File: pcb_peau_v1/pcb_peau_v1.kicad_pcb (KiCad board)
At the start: 2 copper layers, 76 x 74 mm, 27 parts, among them J1 Conn_01x05, J2 Conn_01x05, J4 Conn_02x08_Top_Bottom, J5 Conn_02x12_Top_Bottom, U1 REF200AU, U2 TLC274, U3 CD74HC4067SM, U4 CD74HC4067SM, U5 CD74HC4067SM, U6 CD74HC4067SM, U7 TLC274, U8 TLC274, U9 TLC274

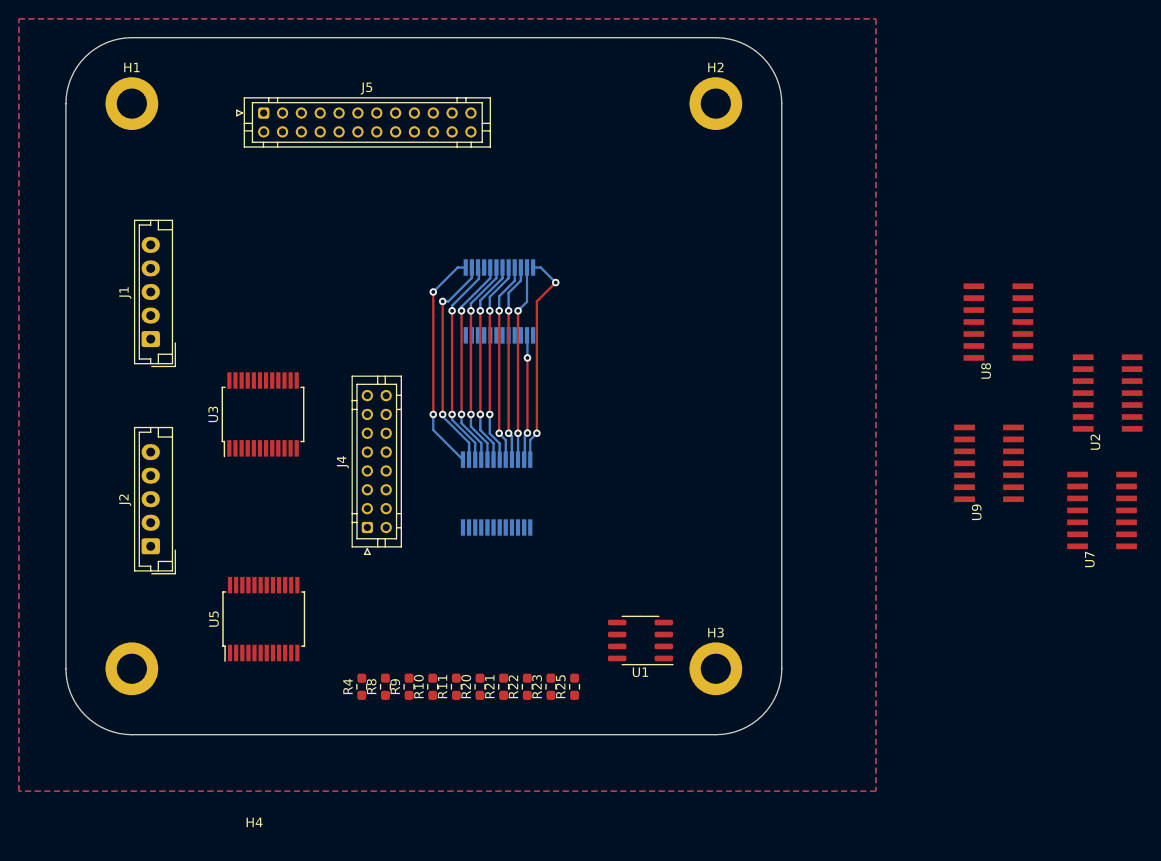
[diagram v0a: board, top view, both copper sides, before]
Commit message: PCB Mux/demux
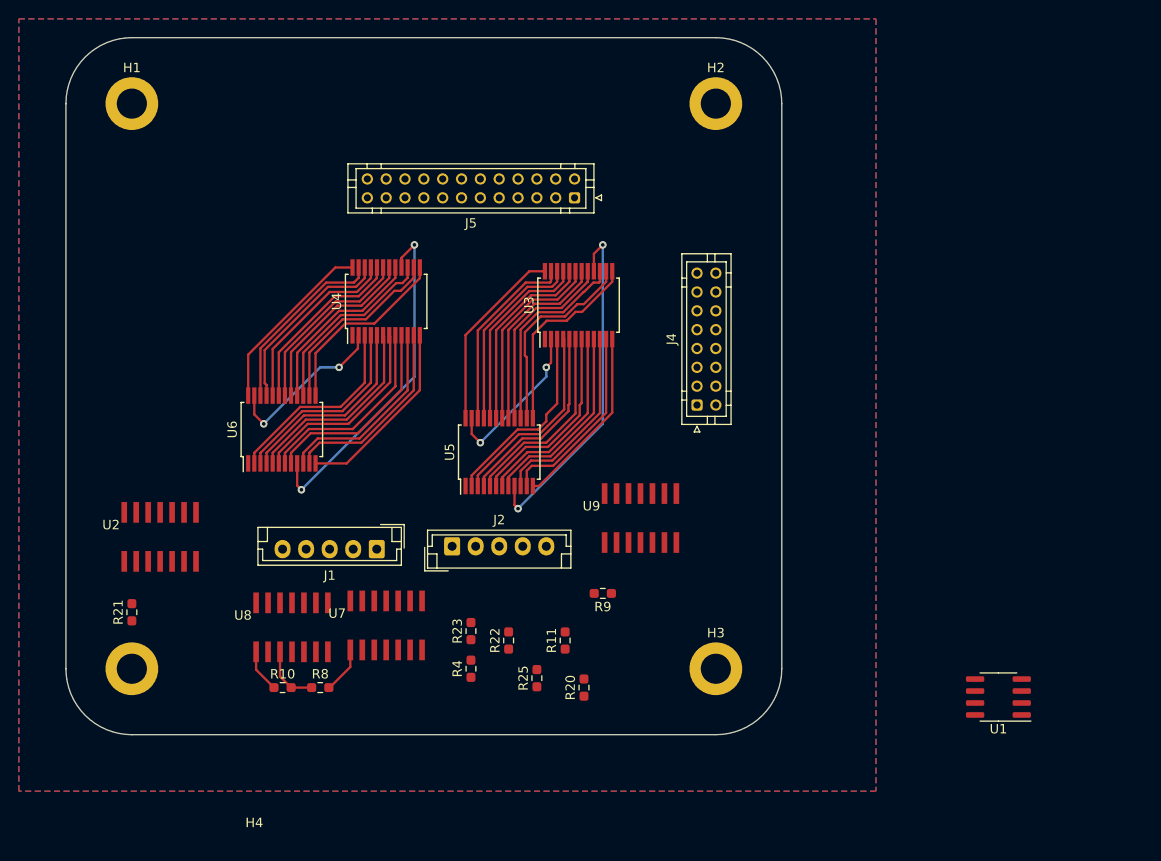
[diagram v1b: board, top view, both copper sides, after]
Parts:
- U4, U6: moved to F.Cu
- moved U2 101.8 mm to (177.0, 96.0), turned to 0 degrees
- moved U8 81.7 mm to (191.0, 105.6), turned to 0 degrees
- moved U7 77.0 mm to (201.0, 105.4), turned to 0 degrees
- moved R21 40.3 mm to (174.0, 104.0)
- moved U1 38.5 mm to (266.0, 113.0)
- moved U9 37.5 mm to (228.0, 94.0), turned to 0 degrees
- moved J4 37.3 mm to (234.0, 82.0)
- moved U3 35.5 mm to (221.4, 71.4)
- moved J5 34.2 mm to (221.0, 60.0), turned to 180 degrees
- moved J1 32.8 mm to (200.0, 97.3), turned to 180 degrees
- moved J2 32.0 mm to (208.0, 97.0), turned to 0 degrees
- moved U5 30.6 mm to (213.0, 87.0)
- moved U6 23.8 mm to (189.9, 84.6)
- moved R9 22.8 mm to (224.0, 102.0), turned to 180 degrees
- moved R10 15.9 mm to (190.0, 112.0), turned to 0 degrees
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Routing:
- net Net-(J4-Pin_1): track 0.00 -> 74.4 mm, vias 0 -> 4
- net Net-(J4-Pin_2): track 0.00 -> 42.1 mm
- net Net-(J4-Pin_3): track 0.00 -> 41.9 mm
- net Net-(J4-Pin_5): track 0.00 -> 41.8 mm
- net Net-(J4-Pin_4): track 0.00 -> 41.8 mm
- net Net-(J4-Pin_7): track 0.00 -> 41.7 mm
- net Net-(J4-Pin_8): track 0.00 -> 41.6 mm
- net Net-(J4-Pin_6): track 0.00 -> 41.5 mm
- net 0: track 0.00 -> 39.6 mm
- net Net-(J4-Pin_9): track 13.4 -> 35.2 mm, vias 2 -> 4
- net C1: track 0.00 -> 21.2 mm
- net NE1: track 0.00 -> 21.0 mm
- net A2: track 0.00 -> 20.8 mm
- net B2: track 0.00 -> 20.8 mm
- net D1: track 0.00 -> 20.7 mm
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
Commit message: PCB avancé
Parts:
- moved J4 24.3 mm to (210.0, 86.0)
- moved U5 8.92 mm to (221.9, 86.3)
- moved U3 8.92 mm to (230.3, 70.7)
- moved U9 8.49 mm to (234.0, 100.0)
- moved U4 1.48 mm to (201.3, 72.5)
- moved U6 1.48 mm to (190.2, 86.0)
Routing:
- net Net-(J4-Pin_7): track 41.7 -> 100.1 mm, vias 0 -> 3
- net Net-(J4-Pin_10): track 40.0 -> 98.1 mm, vias 0 -> 2
- net Net-(J4-Pin_15): track 39.8 -> 91.1 mm, vias 0 -> 2
- net Net-(J4-Pin_4): track 41.8 -> 92.0 mm, vias 0 -> 1
- net Net-(J4-Pin_14): track 39.8 -> 89.4 mm, vias 0 -> 2
- net Net-(J4-Pin_13): track 39.8 -> 89.1 mm, vias 0 -> 2
- net Net-(J4-Pin_5): track 41.8 -> 90.6 mm, vias 0 -> 1
- net Net-(J4-Pin_12): track 40.0 -> 88.2 mm, vias 0 -> 2
- net Net-(J4-Pin_3): track 41.9 -> 89.0 mm
- net Net-(J4-Pin_11): track 40.2 -> 86.9 mm
- net Net-(J4-Pin_8): track 41.6 -> 86.8 mm, vias 0 -> 3
- net Net-(J4-Pin_2): track 42.1 -> 87.2 mm, vias 0 -> 1
- net Net-(J4-Pin_16): track 39.8 -> 84.3 mm, vias 0 -> 2
- net Net-(J4-Pin_9): track 35.2 -> 70.0 mm, vias 4 -> 6
- net Net-(J4-Pin_6): track 41.5 -> 75.6 mm
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
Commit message: fin
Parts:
- removed R20: 1M, Resistor_SMD:R_0603_1608Metric_Pad0.98x0.95mm_HandSolder
- removed U1: REF200AU, Package_SO:SOIC-8_3.9x4.9mm_P1.27mm
- moved R21 48.4 mm to (222.3, 101.4), turned to 0 degrees
- moved J1 33.6 mm to (178.0, 72.0), turned to -90 degrees
- moved J2 32.7 mm to (237.0, 82.0), turned to 90 degrees
- moved J5 30.9 mm to (216.0, 90.5)
- moved U2 26.0 mm to (203.0, 96.5)
- moved R25 23.1 mm to (196.0, 101.5), turned to 180 degrees
- moved R10 15.5 mm to (181.6, 98.9), turned to -90 degrees
- moved R8 15.4 mm to (181.6, 102.9), turned to -90 degrees
- moved R11 10.9 mm to (210.2, 102.3)
- moved R9 9.83 mm to (214.2, 102.4), turned to -90 degrees
- moved R23 9.10 mm to (218.3, 102.4)
- moved U5 8.77 mm to (219.9, 77.7)
- moved U4 8.77 mm to (199.3, 63.9)
- moved J4 8.77 mm to (208.0, 77.5)
- moved U3 8.77 mm to (228.3, 62.1)
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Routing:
- net +5V: track 39.3 -> 190.1 mm, vias 0 -> 7
- net AOP1: track 0.00 -> 85.8 mm, vias 0 -> 4
- net AOP2: track 0.00 -> 66.0 mm, vias 0 -> 2
- net +12V: track 0.00 -> 60.8 mm, vias 0 -> 1
- net -5V: track 0.00 -> 59.5 mm, vias 0 -> 2
- net NE2: track 20.0 -> 74.1 mm, vias 0 -> 3
- net AOP0IN+: track 0.00 -> 52.4 mm, vias 0 -> 1
- net C2: track 20.0 -> 58.6 mm, vias 0 -> 1
- net Net-(U9A-+): track 0.00 -> 33.8 mm
- net Net-(U8A--): track 0.00 -> 30.8 mm, vias 0 -> 2
- net D1: track 20.7 -> 51.3 mm, vias 0 -> 1
- net Net-(U7A-+): track 4.99 -> 33.0 mm, vias 0 -> 2
- net D2: track 20.0 -> 47.6 mm, vias 0 -> 1
- net NE1: track 21.0 -> 46.2 mm, vias 0 -> 1
- net C1: track 21.2 -> 46.3 mm, vias 0 -> 1
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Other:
- board size 76 x 74 mm -> 72.1 x 71 mm

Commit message: PCB corrigé
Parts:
- added R20: 1M, Resistor_SMD:R_0603_1608Metric_Pad0.98x0.95mm_HandSolder, F.Cu at (196.1, 100.0)
- moved H3 1.00 mm to (236.0, 111.0)
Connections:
- J5 pad 10: unconnected-(J5-Pin_10-Pad10) -> C3
- J5 pad 11: unconnected-(J5-Pin_11-Pad11) -> D3
- J5 pad 13: unconnected-(J5-Pin_13-Pad13) -> A4
- J5 pad 14: unconnected-(J5-Pin_14-Pad14) -> B4
- J5 pad 15: unconnected-(J5-Pin_15-Pad15) -> C4
- J5 pad 16: unconnected-(J5-Pin_16-Pad16) -> D4
- J5 pad 8: unconnected-(J5-Pin_8-Pad8) -> A3
- J5 pad 9: unconnected-(J5-Pin_9-Pad9) -> B3
- U3 pad 10: A1 -> A3
- U3 pad 11: B1 -> B3
- U3 pad 13: D1 -> D3
- U3 pad 14: C1 -> C3
- U4 pad 10: A2 -> A4
- U4 pad 11: B2 -> B4
- U4 pad 13: D2 -> D4
- U4 pad 14: C2 -> C4
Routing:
- net D3: track 0.00 -> 58.0 mm, vias 0 -> 1
- net C3: track 0.00 -> 54.9 mm, vias 0 -> 1
- net B3: track 0.00 -> 46.9 mm, vias 0 -> 1
- net A3: track 0.00 -> 41.9 mm, vias 0 -> 2
- net C4: track 0.00 -> 35.5 mm, vias 0 -> 2
- net D4: track 0.00 -> 32.2 mm, vias 0 -> 4
- net A4: track 0.00 -> 25.5 mm
- net B4: track 0.00 -> 22.8 mm
- net D1: track 51.3 -> 28.7 mm
- net B1: track 35.1 -> 14.6 mm
- net A1: track 31.8 -> 11.3 mm
- net C2: track 58.6 -> 38.6 mm
- net Net-(R20-Pad1): track 0.00 -> 19.8 mm, vias 0 -> 2
- net D2: track 47.6 -> 28.2 mm
- net C1: track 46.3 -> 27.8 mm
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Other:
- board size 72.1 x 71 mm -> 70 x 70 mm

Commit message: Modif
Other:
- board text added: "PROJET PEAU_ARTIFICIELLE MITCHEL Maël TCHEGANG YANSE Picard"
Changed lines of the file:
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@@
   (gr_line (start 178 47) (end 236 47)
     (stroke (width 0.1) (type default)) (layer "Edge.Cuts"))
+  (gr_text "PROJET PEAU_ARTIFICIELLE\nMITCHEL Maël\nTCHEGANG YANSE Picard" (at 210 114) (layer "B.Cu")
+    (effects (font (size 1 1) (thickness 0.25) bold) (justify left bottom))
+  )
   (segment (start 203 69.4625) (end 202.848896 69.311396) (width 0.25) (layer "F.Cu") (net 1))
   (segment (start 202.848896 69.311396) (end 202.848896 67.5125) (width 0.25) (layer "F.Cu") (net 1))

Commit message: Pcb Corrigé presque pret
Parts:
- added J3: Conn_01x02, Connector_JST:JST_EH_B2B-EH-A_1x02_P2.50mm_Vertical, F.Cu at (225.1, 110.2)
- moved U7 18.4 mm to (184.7, 101.3)
- moved J5 17.0 mm to (218.7, 73.7)
- moved R8 15.3 mm to (193.0, 113.1)
- moved R10 14.9 mm to (188.5, 112.1)
- moved U2 14.7 mm to (216.9, 101.3)
- moved R20 12.6 mm to (200.7, 111.8)
- moved R25 12.6 mm to (200.6, 113.2)
- moved U8 11.5 mm to (200.9, 101.1), turned to 0 degrees
- moved J4 10.6 mm to (214.1, 86.1), turned to 180 degrees
- moved R21 9.81 mm to (217.9, 110.1), turned to -90 degrees
- moved U4 9.74 mm to (190.5, 59.7)
- moved U9 8.91 mm to (232.7, 101.3)
- moved U5 8.63 mm to (226.3, 83.5)
- moved R11 8.51 mm to (207.3, 110.3)
- moved R23 8.49 mm to (215.1, 110.2)
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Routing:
- net Net-(J4-Pin_9): track 68.5 -> 150.2 mm, vias 6 -> 4
- net Net-(J4-Pin_4): track 91.9 -> 163.2 mm, vias 1 -> 6
- net Net-(J4-Pin_11): track 87.6 -> 141.3 mm, vias 0 -> 7
- net 0: track 45.3 -> 0.00 mm, vias 6 -> 27
- net Net-(J4-Pin_8): track 86.7 -> 128.3 mm, vias 3 -> 5
- net Net-(J4-Pin_6): track 77.2 -> 118.2 mm, vias 0 -> 6
- net Net-(J4-Pin_13): track 90.1 -> 130.3 mm, vias 2 -> 6
- net AOP1: track 85.8 -> 46.0 mm, vias 4 -> 2
- net Net-(J4-Pin_12): track 89.0 -> 125.8 mm, vias 2 -> 5
- net TRIOAOP1: track 26.6 -> 60.0 mm
- net Net-(J4-Pin_15): track 92.3 -> 122.4 mm, vias 2 -> 3
- net NE2: track 74.1 -> 44.6 mm, vias 3 -> 2
- net Net-(J4-Pin_7): track 99.9 -> 129.3 mm, vias 3 -> 5
- net Net-(J4-Pin_5): track 93.3 -> 121.5 mm, vias 3 -> 7
- net Net-(J4-Pin_10): track 90.4 -> 116.2 mm, vias 3 -> 5
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
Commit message: modif
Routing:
- net Net-(J4-Pin_16): track 103.2 -> 105.8 mm, vias 5 -> 7
- net Net-(R20-Pad1): track 9.64 -> 11.6 mm, vias 0 -> 2

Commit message: PCB au bonnes normes (on y croit)
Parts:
- moved U4 5.16 mm to (191.4, 54.6)
- moved U7 5.11 mm to (179.6, 100.8)
- moved U3 5.02 mm to (224.4, 54.6)
- moved H4 3.91 mm to (175.3, 113.8)
- moved H3 3.75 mm to (238.5, 113.8)
- moved H1 3.68 mm to (175.3, 50.5)
- moved H2 3.51 mm to (238.5, 50.5)
- moved J1 3.41 mm to (175.3, 74.0)
- moved U9 3.34 mm to (236.0, 100.8)
- moved J2 3.20 mm to (240.1, 82.9)
- moved U8 2.81 mm to (198.1, 100.8)
- moved R11 2.55 mm to (206.7, 112.8)
- moved R4 2.55 mm to (212.1, 116.3)
- moved J3 2.55 mm to (224.6, 112.7)
- moved R10 2.55 mm to (187.9, 114.6)
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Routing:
- net Net-(J4-Pin_3): track 96.3 -> 187.5 mm, vias 5 -> 10
- net -5V: track 67.7 -> 106.2 mm, vias 2 -> 3
- net Net-(J4-Pin_13): track 130.3 -> 166.5 mm, vias 6 -> 5
- net Net-(J4-Pin_2): track 108.3 -> 141.9 mm, vias 7 -> 9
- net Net-(J4-Pin_4): track 163.2 -> 132.4 mm
- net Net-(J4-Pin_8): track 128.3 -> 158.0 mm, vias 5 -> 7
- net C1: track 48.1 -> 22.3 mm
- net Net-(J4-Pin_1): track 132.5 -> 158.0 mm, vias 3 -> 2
- net Net-(J4-Pin_5): track 121.5 -> 145.3 mm
- net Net-(J4-Pin_14): track 114.9 -> 138.0 mm
- net Net-(J4-Pin_10): track 116.2 -> 134.1 mm, vias 5 -> 3
- net Net-(J4-Pin_11): track 141.3 -> 158.3 mm, vias 7 -> 4
- net 2-ENTREE: track 25.6 -> 42.5 mm, vias 1 -> 2
- net Net-(J4-Pin_16): track 105.8 -> 122.7 mm, vias 7 -> 4
- net Net-(J4-Pin_9): track 150.2 -> 167.0 mm
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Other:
- board size 70 x 70 mm -> 79.5 x 79.5 mm
